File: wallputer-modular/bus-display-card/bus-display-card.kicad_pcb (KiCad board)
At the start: 2 copper layers, 99.7 x 99.7 mm, 1 part

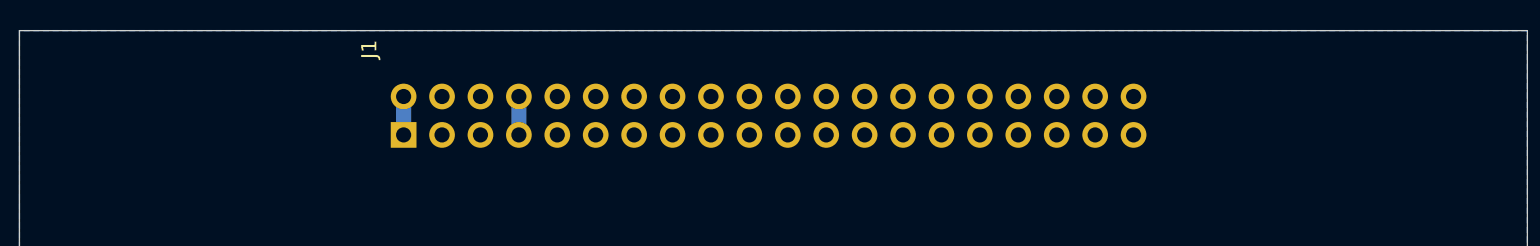
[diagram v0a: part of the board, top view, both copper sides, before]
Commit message: add card name
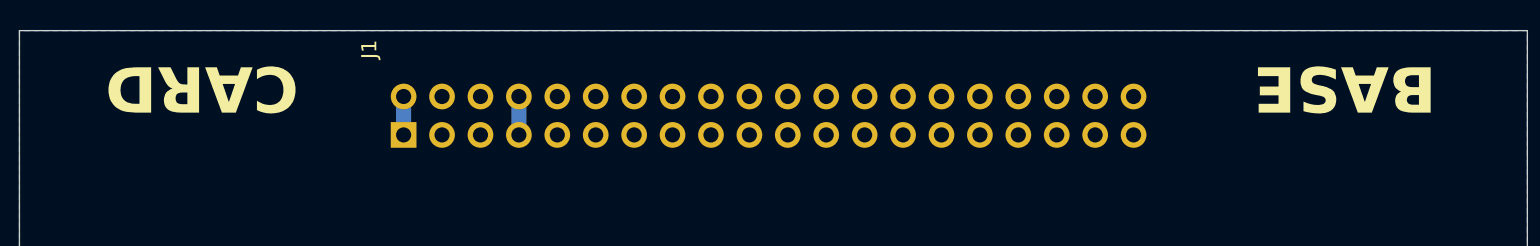
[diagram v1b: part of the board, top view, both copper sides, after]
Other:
- board text added: "BASE"
- board text added: "CARD"
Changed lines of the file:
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@@
 		(layer "Edge.Cuts")
+	)
+	(gr_text "BASE"
+		(at 151.13 67.31 180)
+		(layer "F.SilkS")
+		(effects
+			(font
+				(size 3 3)
+				(thickness 0.5)
+				(bold yes)
+			)
+		)
+	)
+	(gr_text "CARD\n"
+		(at 75.565 67.31 180)
+		(layer "F.SilkS")
+		(effects
+			(font
+				(size 3 3)
+				(thickness 0.5)
+				(bold yes)
+			)
+		)
 	)
 	(segment

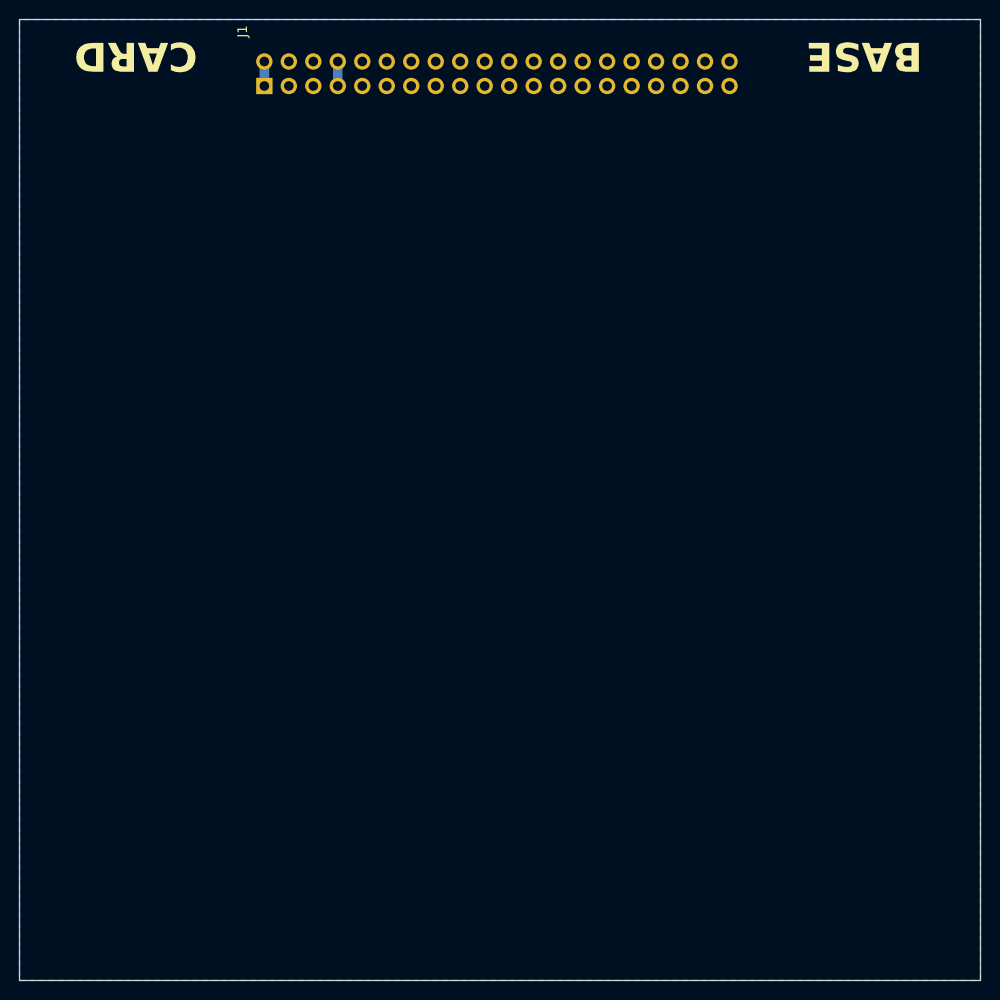
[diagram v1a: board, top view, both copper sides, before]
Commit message: bus display PCB
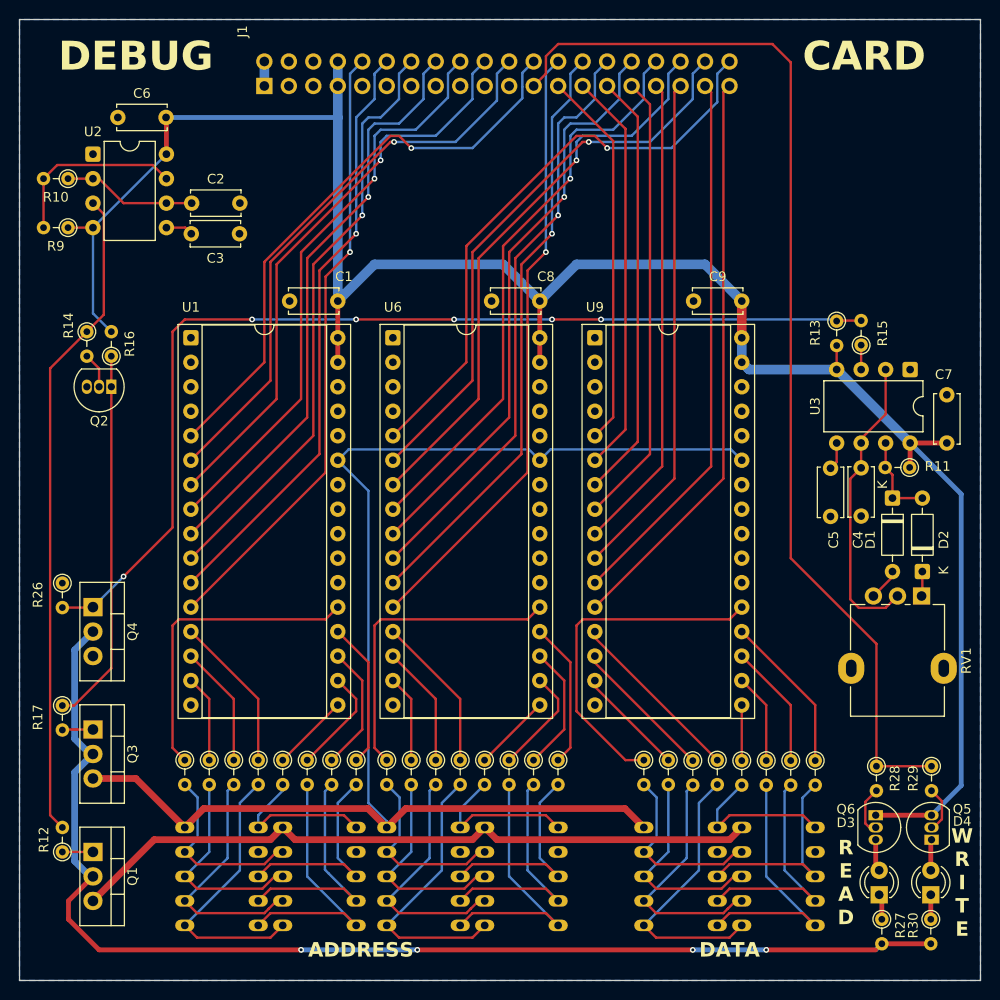
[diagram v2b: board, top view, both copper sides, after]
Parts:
- added C1: 100nF, Capacitor_THT:C_Disc_D5.0mm_W2.5mm_P5.00mm, F.Cu at (96.5, 92.7)
- added C2: 10n, Capacitor_THT:C_Disc_D5.0mm_W2.5mm_P5.00mm, F.Cu at (81.4, 82.5)
- added C3: 10p, Capacitor_THT:C_Disc_D5.0mm_W2.5mm_P5.00mm, F.Cu at (81.3, 85.7)
- added C4: 4.7nF, Capacitor_THT:C_Disc_D5.0mm_W2.5mm_P5.00mm, F.Cu at (150.8, 110.0)
- added C5: 0.01uF, Capacitor_THT:C_Disc_D5.0mm_W2.5mm_P5.00mm, F.Cu at (147.6, 115.1)
- added C6: 100nF, Capacitor_THT:C_Disc_D5.0mm_W2.5mm_P5.00mm, F.Cu at (73.7, 73.7)
- added C7: 100nF, Capacitor_THT:C_Disc_D5.0mm_W2.5mm_P5.00mm, F.Cu at (159.7, 107.4)
- added C8: 100nF, Capacitor_THT:C_Disc_D5.0mm_W2.5mm_P5.00mm, F.Cu at (117.5, 92.7)
- added C9: 100nF, Capacitor_THT:C_Disc_D5.0mm_W2.5mm_P5.00mm, F.Cu at (138.4, 92.7)
- added D1: 1n4148, Diode_THT:D_DO-35_SOD27_P7.62mm_Horizontal, F.Cu at (154.1, 113.2)
- added D2: 1n4148, Diode_THT:D_DO-35_SOD27_P7.62mm_Horizontal, F.Cu at (157.2, 120.8)
- added D3: Green, LED_THT:LED_D3.0mm, F.Cu at (152.7, 154.3)
- added D4: Red, LED_THT:LED_D3.0mm, F.Cu at (158.0, 154.3)
- added Q1: IRLZ44N, Package_TO_SOT_THT:TO-220-3_Vertical, F.Cu at (71.1, 149.9)
- added Q2: BC547, Package_TO_SOT_THT:TO-92_Inline, F.Cu at (73.0, 101.6)
- added Q3: IRLZ44N, Package_TO_SOT_THT:TO-220-3_Vertical, F.Cu at (71.1, 137.2)
- added Q4: IRLZ44N, Package_TO_SOT_THT:TO-220-3_Vertical, F.Cu at (71.1, 124.5)
- added Q5: BC547, Package_TO_SOT_THT:TO-92_Inline, F.Cu at (152.3, 146.1)
- added Q6: BC557, Package_TO_SOT_THT:TO-92_Inline, F.Cu at (158.1, 148.6)
- added R1: 220, Resistor_THT:R_Axial_DIN0204_L3.6mm_D1.6mm_P2.54mm_Vertical, F.Cu at (88.3, 140.3)
- added R10: 100k, Resistor_THT:R_Axial_DIN0204_L3.6mm_D1.6mm_P2.54mm_Vertical, F.Cu at (68.5, 80.0)
- added R11: 1k, Resistor_THT:R_Axial_DIN0204_L3.6mm_D1.6mm_P2.54mm_Vertical, F.Cu at (155.8, 110.0)
- added R12: 100, Resistor_THT:R_Axial_DIN0204_L3.6mm_D1.6mm_P2.54mm_Vertical, F.Cu at (67.9, 149.9)
- added R13: 220, Resistor_THT:R_Axial_DIN0204_L3.6mm_D1.6mm_P2.54mm_Vertical, F.Cu at (150.8, 97.3)
- added R14: 10k, Resistor_THT:R_Axial_DIN0204_L3.6mm_D1.6mm_P2.54mm_Vertical, F.Cu at (70.5, 95.9)
- added R15: 10k, Resistor_THT:R_Axial_DIN0204_L3.6mm_D1.6mm_P2.54mm_Vertical, F.Cu at (148.3, 94.8)
- added R16: 10k, Resistor_THT:R_Axial_DIN0204_L3.6mm_D1.6mm_P2.54mm_Vertical, F.Cu at (73.0, 98.4)
- added R17: 100, Resistor_THT:R_Axial_DIN0204_L3.6mm_D1.6mm_P2.54mm_Vertical, F.Cu at (67.9, 134.7)
- added R18: 220, Resistor_THT:R_Axial_DIN0204_L3.6mm_D1.6mm_P2.54mm_Vertical, F.Cu at (109.2, 140.3)
- added R19: 220, Resistor_THT:R_Axial_DIN0204_L3.6mm_D1.6mm_P2.54mm_Vertical, F.Cu at (106.7, 140.3)
- added R2: 220, Resistor_THT:R_Axial_DIN0204_L3.6mm_D1.6mm_P2.54mm_Vertical, F.Cu at (85.7, 140.3)
- added R20: 220, Resistor_THT:R_Axial_DIN0204_L3.6mm_D1.6mm_P2.54mm_Vertical, F.Cu at (104.1, 140.3)
- added R21: 220, Resistor_THT:R_Axial_DIN0204_L3.6mm_D1.6mm_P2.54mm_Vertical, F.Cu at (111.7, 140.3)
- added R22: 220, Resistor_THT:R_Axial_DIN0204_L3.6mm_D1.6mm_P2.54mm_Vertical, F.Cu at (114.3, 140.3)
- added R23: 220, Resistor_THT:R_Axial_DIN0204_L3.6mm_D1.6mm_P2.54mm_Vertical, F.Cu at (116.8, 140.3)
- added R24: 220, Resistor_THT:R_Axial_DIN0204_L3.6mm_D1.6mm_P2.54mm_Vertical, F.Cu at (119.4, 140.3)
- added R25: 220, Resistor_THT:R_Axial_DIN0204_L3.6mm_D1.6mm_P2.54mm_Vertical, F.Cu at (101.6, 140.3)
- added R26: 100k, Resistor_THT:R_Axial_DIN0204_L3.6mm_D1.6mm_P2.54mm_Vertical, F.Cu at (67.9, 122.0)
- added R27: 220, Resistor_THT:R_Axial_DIN0204_L3.6mm_D1.6mm_P2.54mm_Vertical, F.Cu at (153.0, 156.8)
- added R28: 10k, Resistor_THT:R_Axial_DIN0204_L3.6mm_D1.6mm_P2.54mm_Vertical, F.Cu at (152.4, 141.0)
- added R29: 10k, Resistor_THT:R_Axial_DIN0204_L3.6mm_D1.6mm_P2.54mm_Vertical, F.Cu at (158.1, 141.0)
- added R3: 220, Resistor_THT:R_Axial_DIN0204_L3.6mm_D1.6mm_P2.54mm_Vertical, F.Cu at (83.2, 140.3)
- added R30: 220, Resistor_THT:R_Axial_DIN0204_L3.6mm_D1.6mm_P2.54mm_Vertical, F.Cu at (158.0, 156.8)
- added R31: 220, Resistor_THT:R_Axial_DIN0204_L3.6mm_D1.6mm_P2.54mm_Vertical, F.Cu at (135.9, 140.3)
- added R32: 220, Resistor_THT:R_Axial_DIN0204_L3.6mm_D1.6mm_P2.54mm_Vertical, F.Cu at (133.3, 140.4)
- added R33: 220, Resistor_THT:R_Axial_DIN0204_L3.6mm_D1.6mm_P2.54mm_Vertical, F.Cu at (130.8, 140.3)
- added R34: 220, Resistor_THT:R_Axial_DIN0204_L3.6mm_D1.6mm_P2.54mm_Vertical, F.Cu at (138.4, 140.4)
- added R35: 220, Resistor_THT:R_Axial_DIN0204_L3.6mm_D1.6mm_P2.54mm_Vertical, F.Cu at (141.0, 140.4)
- added R36: 220, Resistor_THT:R_Axial_DIN0204_L3.6mm_D1.6mm_P2.54mm_Vertical, F.Cu at (143.5, 140.4)
- added R37: 220, Resistor_THT:R_Axial_DIN0204_L3.6mm_D1.6mm_P2.54mm_Vertical, F.Cu at (146.1, 140.4)
- added R38: 220, Resistor_THT:R_Axial_DIN0204_L3.6mm_D1.6mm_P2.54mm_Vertical, F.Cu at (128.3, 140.3)
- added R4: 220, Resistor_THT:R_Axial_DIN0204_L3.6mm_D1.6mm_P2.54mm_Vertical, F.Cu at (90.8, 140.3)
- added R5: 220, Resistor_THT:R_Axial_DIN0204_L3.6mm_D1.6mm_P2.54mm_Vertical, F.Cu at (93.3, 140.3)
- added R6: 220, Resistor_THT:R_Axial_DIN0204_L3.6mm_D1.6mm_P2.54mm_Vertical, F.Cu at (95.9, 140.3)
- added R7: 220, Resistor_THT:R_Axial_DIN0204_L3.6mm_D1.6mm_P2.54mm_Vertical, F.Cu at (98.4, 140.3)
- added R8: 220, Resistor_THT:R_Axial_DIN0204_L3.6mm_D1.6mm_P2.54mm_Vertical, F.Cu at (80.6, 140.3)
- added R9: 1k, Resistor_THT:R_Axial_DIN0204_L3.6mm_D1.6mm_P2.54mm_Vertical, F.Cu at (68.5, 85.1)
- added RV1: 50k, Potentiometer_THT:Potentiometer_Alpha_RD901F-40-00D_Single_Vertical, F.Cu at (157.1, 123.3)
- added U1: SST39SF010, Package_DIP:DIP-32_W15.24mm_Socket, F.Cu at (81.3, 96.5)
- added U10: INND-TS40, Wallputer:INND-TS40, F.Cu at (132.1, 152.4)
- added U11: INND-TS40, Wallputer:INND-TS40, F.Cu at (142.2, 152.4)
- added U2: NE555P, Package_DIP:DIP-8_W7.62mm, F.Cu at (71.1, 77.5)
- added U3: TLC555CD, Package_DIP:DIP-8_W7.62mm, F.Cu at (155.9, 99.8)
- added U4: INND-TS40, Wallputer:INND-TS40, F.Cu at (84.5, 152.4)
- added U5: INND-TS40, Wallputer:INND-TS40, F.Cu at (94.6, 152.4)
- added U6: SST39SF010, Package_DIP:DIP-32_W15.24mm_Socket, F.Cu at (102.2, 96.5)
- added U7: INND-TS40, Wallputer:INND-TS40, F.Cu at (105.4, 152.4)
- added U8: INND-TS40, Wallputer:INND-TS40, F.Cu at (115.6, 152.4)
- added U9: SST39SF010, Package_DIP:DIP-32_W15.24mm_Socket, F.Cu at (123.2, 96.5)
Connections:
- J1 pad 10: unconnected-(J1-A5-Pad10) -> /A5
- J1 pad 11: unconnected-(J1-A6-Pad11) -> /A6
- J1 pad 12: unconnected-(J1-A7-Pad12) -> /A7
- J1 pad 13: unconnected-(J1-A8-Pad13) -> /A8
- J1 pad 14: unconnected-(J1-A9-Pad14) -> /A9
- J1 pad 15: unconnected-(J1-A10-Pad15) -> /A10
- J1 pad 16: unconnected-(J1-A11-Pad16) -> /A11
- J1 pad 17: unconnected-(J1-A12-Pad17) -> /A12
- J1 pad 18: unconnected-(J1-A13-Pad18) -> /A13
- J1 pad 19: unconnected-(J1-A14-Pad19) -> /A14
- J1 pad 20: unconnected-(J1-A15-Pad20) -> /A15
- J1 pad 21: unconnected-(J1-D0-Pad21) -> /D0
- J1 pad 22: unconnected-(J1-D1-Pad22) -> /D1
- J1 pad 23: unconnected-(J1-D2-Pad23) -> /D2
- J1 pad 24: unconnected-(J1-D3-Pad24) -> /D3
- J1 pad 25: unconnected-(J1-D4-Pad25) -> /D4
- J1 pad 26: unconnected-(J1-D5-Pad26) -> /D5
- J1 pad 27: unconnected-(J1-D6-Pad27) -> /D6
- J1 pad 28: unconnected-(J1-D7-Pad28) -> /D7
- J1 pad 29: unconnected-(J1-RW/-Pad29) -> RW/
- J1 pad 5: unconnected-(J1-A0-Pad5) -> /A0
- J1 pad 6: unconnected-(J1-A1-Pad6) -> /A1
- J1 pad 7: unconnected-(J1-A2-Pad7) -> /A2
- J1 pad 8: unconnected-(J1-A3-Pad8) -> /A3
- J1 pad 9: unconnected-(J1-A4-Pad9) -> /A4
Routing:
- net +5V: track 2.54 -> 216.4 mm
- net Net-(Q3-S): track 0.00 -> 146.5 mm
- net Net-(Q1-D): track 0.00 -> 125.5 mm, vias 0 -> 4
- net RW/: track 0.00 -> 112.7 mm
- net SW_BUS_LED: track 0.00 -> 107.2 mm, vias 0 -> 6
- net Net-(Q1-S): track 0.00 -> 72.6 mm
- net Net-(U2-Q): track 0.00 -> 68.1 mm
- net /A0: track 0.00 -> 64.0 mm, vias 0 -> 1
- net /A8: track 0.00 -> 63.7 mm, vias 0 -> 1
- net /A1: track 0.00 -> 62.5 mm, vias 0 -> 1
- net /A9: track 0.00 -> 62.2 mm, vias 0 -> 1
- net /A2: track 0.00 -> 61.7 mm, vias 0 -> 1
- net /A10: track 0.00 -> 61.5 mm, vias 0 -> 1
- net /A3: track 0.00 -> 61.0 mm, vias 0 -> 1
- net /A15: track 0.00 -> 60.8 mm, vias 0 -> 1
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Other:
- board text added: "ADDRESS"
- board text added: "DATA"
- board text added: "DEBUG"
- board text added: "R E A D"
- board text added: "W R I T E"
- board text removed: "BASE"
